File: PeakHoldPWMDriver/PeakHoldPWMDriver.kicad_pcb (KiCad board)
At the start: 2 copper layers, 74 parts, among them Q1 BSP78, Q16 SMD-MOSFET-N-CH-55V-2.1A-AO34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, Q17 TSM2309CX, Q19 SMD-MOSFET-N-CH-55V-2.1A-AO34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, Q2 BSP78, Q20 TSM2309CX, Q21 SMD-MOSFET-N-CH-55V-2.1A-AO34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, Q22 SMD-MOSFET-N-CH-55V-2.1A-AO34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, Q23 TSM2309CX, Q24 TSM2309CX, Q3 BSP78, Q4 BSP78, U1 LM2901, U10 74LS08, U2 74LS08, U3 LM78M05_TO220, U4 74HC74, U5 74LS08, U6 LTC6992, U7 74LS08, U8 74LS08, U9 74LS08

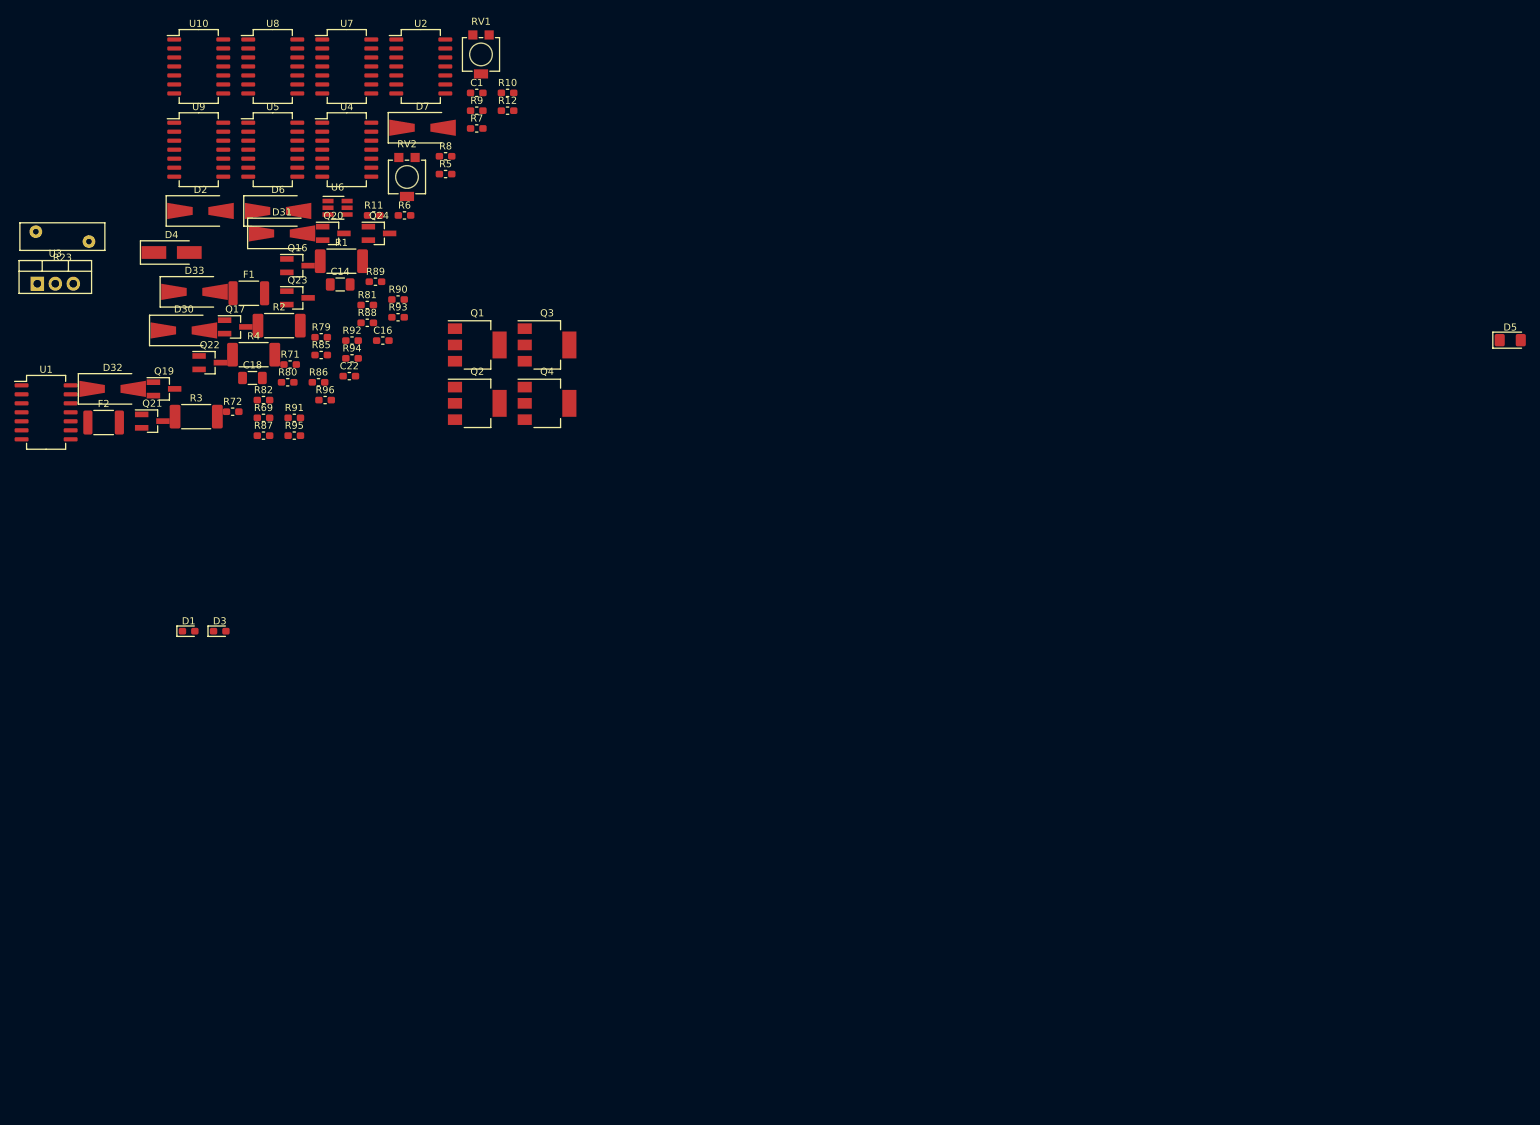
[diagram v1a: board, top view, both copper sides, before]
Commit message: Cleaned and updated the SPECTRE V0.5 Created separate Peak and Hold board.
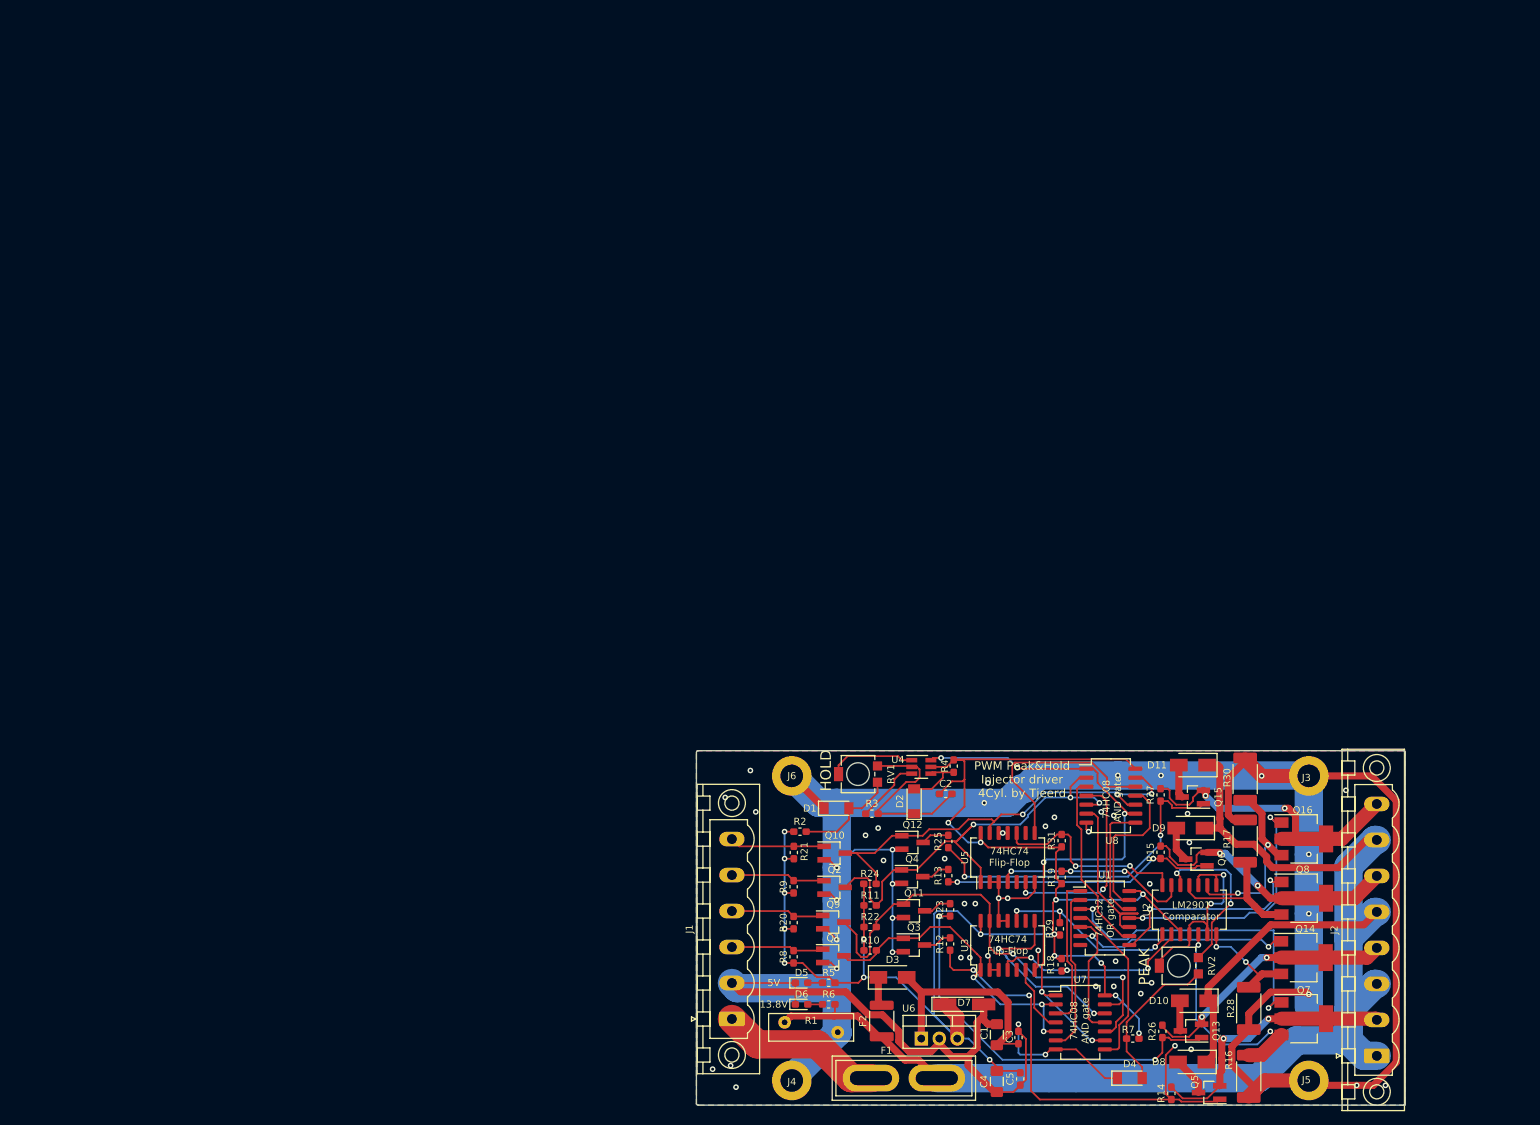
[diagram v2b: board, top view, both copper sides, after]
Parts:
- removed the D1 at (40.1, 49.2)
- removed the D2 at (41.7, -10.2)
- removed D30, D31, D32, D33: SS310, Diode_SMD:D_SMA-SMB_Universal_Handsoldering
- removed the F2 at (28.1, 19.7)
- removed Q17, Q20, Q23, Q24: TSM2309CX, Package_TO_SOT_SMD:SOT-23_Handsoldering
- removed Q19: SMD-MOSFET-N-CH-55V-2.1A-AO3422(SOT-23), Package_TO_SOT_SMD:SOT-23_Handsoldering
- removed the Q4 at (90.7, 17.0)
- removed the R1 at (61.6, -3.07)
- removed the R2 at (52.8, 6.03)
- removed the R3 at (41.1, 18.9)
- removed R72: 0R0, Resistor_SMD:R_0603_1608Metric_Pad1.05x0.95mm_HandSolder
- removed R79, R88, R95, R96: 10k, Resistor_SMD:R_0603_1608Metric_Pad1.05x0.95mm_HandSolder
- removed R80, R85, R89, R90: 1K, Resistor_SMD:R_0603_1608Metric_Pad1.05x0.95mm_HandSolder
- removed R81, R86, R91, R93: 470, Resistor_SMD:R_0603_1608Metric_Pad1.05x0.95mm_HandSolder
- removed R82, R87: 1K8, Resistor_SMD:R_0603_1608Metric_Pad1.05x0.95mm_HandSolder
- removed U10, U9: 74LS08, Package_SO:SO-14_5.3x10.2mm_P1.27mm
- removed the U2 at (72.8, -30.6)
- removed the U4 at (62.4, -18.8)
- removed the U8 at (51.9, -30.6)
- added D10: SS310, Diode_SMD:D_SMA, F.Cu at (182.0, 101.3)
- added D11: SS310, Diode_SMD:D_SMA, F.Cu at (181.9, 68.1)
- added D6: BLUE, LED_SMD:LED_0603_1608Metric_Pad1.05x0.95mm_HandSolder, F.Cu at (126.6, 101.9)
- added D7: D_Zener_Small, Diode_SMD:D_MiniMELF_Handsoldering, F.Cu at (149.6, 101.9)
- added D8: SS310, Diode_SMD:D_SMA, F.Cu at (181.8, 110.0)
- added D9: SS310, Diode_SMD:D_SMA, F.Cu at (181.5, 77.0)
- added F1: Fuse, Fuse:Fuse_Blade_ATO_directSolder, F.Cu at (136.4, 112.3)
- added J1: Screw_Terminal_01x06, Connector_Phoenix_MSTB:PhoenixContact_MSTBV_2,5_6-GF-5,08_1x06_P5.08mm_Vertical_ThreadedFlange, F.Cu at (116.8, 103.9)
- added J2: Screw_Terminal_01x08, Connector_Phoenix_MSTB:PhoenixContact_MSTBV_2,5_8-GF-5,08_1x08_P5.08mm_Vertical_ThreadedFlange, F.Cu at (207.8, 109.1)
- added J3: Mounting 3mm, MountingHole:MountingHole_3.2mm_M3_DIN965_Pad, F.Cu at (198.2, 69.6)
- added J4: Mounting 3mm, MountingHole:MountingHole_3.2mm_M3_DIN965_Pad, F.Cu at (125.2, 112.6)
- added J5: Mounting 3mm, MountingHole:MountingHole_3.2mm_M3_DIN965_Pad, F.Cu at (198.2, 112.6)
- added J6: Mounting 3mm, MountingHole:MountingHole_3.2mm_M3_DIN965_Pad, F.Cu at (125.2, 69.6)
- added Q10: AO3400, Package_TO_SOT_SMD:SOT-23_Handsoldering, F.Cu at (131.3, 80.5)
- added Q13: AO3401A, Package_TO_SOT_SMD:SOT-23_Handsoldering, F.Cu at (181.6, 105.6)
- added Q14: BSP78, Package_TO_SOT_SMD:SOT-223, F.Cu at (197.5, 95.2)
- added Q15: AO3401A, Package_TO_SOT_SMD:SOT-23_Handsoldering, F.Cu at (181.8, 72.6)
- added Q16: BSP78, Package_TO_SOT_SMD:SOT-223, F.Cu at (197.5, 78.5)
- added Q5: AO3401A, Package_TO_SOT_SMD:SOT-23_Handsoldering, F.Cu at (184.2, 114.3)
- added Q6: AO3401A, Package_TO_SOT_SMD:SOT-23_Handsoldering, F.Cu at (182.3, 81.3)
- added Q7: BSP78, Package_TO_SOT_SMD:SOT-223, F.Cu at (197.5, 103.9)
- added Q8: BSP78, Package_TO_SOT_SMD:SOT-223, F.Cu at (197.5, 86.9)
- added Q9: AO3400, Package_TO_SOT_SMD:SOT-23_Handsoldering, F.Cu at (131.1, 90.2)
- added R10: 10K, Resistor_SMD:R_0603_1608Metric_Pad1.05x0.95mm_HandSolder, F.Cu at (136.3, 94.2)
- added R11: 10K, Resistor_SMD:R_0603_1608Metric_Pad1.05x0.95mm_HandSolder, F.Cu at (136.3, 87.9)
- added R12: 1K8, Resistor_SMD:R_0603_1608Metric_Pad1.05x0.95mm_HandSolder, F.Cu at (147.6, 93.3)
- added R13: 1K8, Resistor_SMD:R_0603_1608Metric_Pad1.05x0.95mm_HandSolder, F.Cu at (147.3, 83.7)
- added R14: 470, Resistor_SMD:R_0603_1608Metric_Pad1.05x0.95mm_HandSolder, F.Cu at (178.8, 114.4)
- added R15: 470, Resistor_SMD:R_0603_1608Metric_Pad1.05x0.95mm_HandSolder, F.Cu at (177.3, 80.4)
- added R16: 0R1, Resistor_SMD:R_2512_6332Metric_Pad1.52x3.35mm_HandSolder, F.Cu at (189.7, 112.0)
- added R17: 0R1, Resistor_SMD:R_2512_6332Metric_Pad1.52x3.35mm_HandSolder, F.Cu at (189.2, 78.8)
- added R20: 1K, Resistor_SMD:R_0603_1608Metric_Pad1.05x0.95mm_HandSolder, F.Cu at (125.5, 90.3)
- added R21: 1K, Resistor_SMD:R_0603_1608Metric_Pad1.05x0.95mm_HandSolder, F.Cu at (125.5, 80.4)
- added R22: 10K, Resistor_SMD:R_0603_1608Metric_Pad1.05x0.95mm_HandSolder, F.Cu at (136.3, 90.9)
- added R24: 10K, Resistor_SMD:R_0603_1608Metric_Pad1.05x0.95mm_HandSolder, F.Cu at (136.3, 84.8)
- added R26: 470, Resistor_SMD:R_0603_1608Metric_Pad1.05x0.95mm_HandSolder, F.Cu at (177.5, 105.7)
- added R27: 470, Resistor_SMD:R_0603_1608Metric_Pad1.05x0.95mm_HandSolder, F.Cu at (177.3, 72.3)
- added R28: 0R1, Resistor_SMD:R_2512_6332Metric_Pad1.52x3.35mm_HandSolder, F.Cu at (189.7, 102.4)
- added R30: 0R1, Resistor_SMD:R_2512_6332Metric_Pad1.52x3.35mm_HandSolder, F.Cu at (189.2, 70.0)
- added R9: 1K, Resistor_SMD:R_0603_1608Metric_Pad1.05x0.95mm_HandSolder, F.Cu at (125.5, 85.3)
- added U3: 74LS74, Package_SO:SO-14_5.3x10.2mm_P1.27mm, F.Cu at (155.7, 93.5)
- added U5: 74LS74, Package_SO:SO-14_5.3x10.2mm_P1.27mm, F.Cu at (155.7, 81.1)
- added U7: 74LS08, Package_SO:SO-14_5.3x10.2mm_P1.27mm, F.Cu at (166.0, 104.4)
- C1: renamed from C14; footprint Capacitor_SMD:C_1206_3216Metric -> Capacitor_SMD:C_1206_3216Metric_Pad1.42x1.75mm_HandSolder
- C4: renamed from C18; footprint Capacitor_SMD:C_1206_3216Metric -> Capacitor_SMD:C_1206_3216Metric_Pad1.42x1.75mm_HandSolder
- D1: renamed from D6; value SS310 -> LL4148; footprint Diode_SMD:D_SMA-SMB_Universal_Handsoldering -> Diode_SMD:D_MiniMELF
- D2: renamed from D7; footprint Diode_SMD:D_SMA-SMB_Universal_Handsoldering -> Diode_SMD:D_MiniMELF
- D3: value BLUE -> 40V-1A; footprint LED_SMD:LED_0603_1608Metric_Pad1.05x0.95mm_HandSolder -> Diode_SMD:D_SMA
- D4: value D -> LL4148; footprint Diode_SMD:D_SMA_Handsoldering -> Diode_SMD:D_MiniMELF
- D5: value 5V1 -> BLUE; footprint Diode_SMD:D_1206_3216Metric_Pad1.42x1.75mm_HandSolder -> LED_SMD:LED_0603_1608Metric_Pad1.05x0.95mm_HandSolder
- F2: renamed from F1; footprint Resistor_SMD:R_1812_4532Metric_Pad1.30x3.40mm_HandSolder -> Fuse:Fuse_1812_4532Metric_Pad1.30x3.40mm_HandSolder
- Q1, Q2: value BSP78 -> AO3400; footprint Package_TO_SOT_SMD:SOT-223-3_TabPin2 -> Package_TO_SOT_SMD:SOT-23_Handsoldering
- Q11: renamed from Q21; value SMD-MOSFET-N-CH-55V-2.1A-AO3422(SOT-23) -> AO3422
- Q12: renamed from Q22; value SMD-MOSFET-N-CH-55V-2.1A-AO3422(SOT-23) -> AO3422
- Q3: value BSP78 -> AO3422; footprint Package_TO_SOT_SMD:SOT-223-3_TabPin2 -> Package_TO_SOT_SMD:SOT-23_Handsoldering
- Q4: renamed from Q16; value SMD-MOSFET-N-CH-55V-2.1A-AO3422(SOT-23) -> AO3422
- R4: value 0R1 -> 500k; footprint Resistor_SMD:R_2512_6332Metric_Pad1.52x3.35mm_HandSolder -> Resistor_SMD:R_0603_1608Metric_Pad1.05x0.95mm_HandSolder
- R8: value 500k -> 1K
- U1: renamed from U7; value 74LS08 -> 74LS32
- moved D4 178.6 mm to (172.9, 112.3)
- moved U2 176.0 mm to (181.4, 88.5), turned to 90 degrees
- moved U6 164.1 mm to (143.5, 106.7)
- moved RV2 162.1 mm to (179.9, 96.4), turned to 270 degrees
- moved U1 161.0 mm to (169.4, 89.7)
- moved R1 160.0 mm to (131.7, 105.8), turned to 180 degrees
- moved R7 155.9 mm to (173.4, 106.7), turned to 180 degrees
- moved U8 149.4 mm to (170.3, 72.4)
- moved R18 146.2 mm to (163.3, 96.3), turned to 270 degrees
- moved C4 144.6 mm to (154.2, 112.7), turned to 90 degrees
- moved C1 140.8 mm to (154.2, 106.1), turned to 270 degrees
- moved R29 139.7 mm to (163.1, 91.2), turned to 90 degrees
- moved C5 137.2 mm to (157.5, 112.4), turned to 90 degrees
- moved F2 136.2 mm to (137.9, 104.2), turned to 90 degrees
- moved R19 135.6 mm to (163.3, 83.9), turned to 90 degrees
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- renumbered C1 to C2, C16 to C3, C22 to C5, R23 to R1, R9 to R18, R10 to R19, R6 to R2, R92 to R23, R94 to R25, R11 to R29, R7 to R3, R12 to R31, R69 to R5, R71 to R6, R5 to R7, RV2 to RV1, RV1 to RV2, U1 to U2, U6 to U4, U3 to U6, U5 to U8
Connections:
- C1 pad 1: GND -> PWR_GND
- C1 pad 2: Net-(C14-Pad2) -> Net-(C1-Pad2)
- C2 pad 2: GND -> PWR_GND
- C3 pad 1: GND -> PWR_GND
- C3 pad 2: Net-(C14-Pad2) -> Net-(C1-Pad2)
- C4 pad 1: GND -> PWR_GND
- C5 pad 1: GND -> PWR_GND
- D1 pad 1: GND -> PWR_GND
- D2 pad 1: GND -> PWR_GND
- D2 pad 2: Net-(D7-Pad2) -> Net-(D2-Pad2)
- D3 pad 1: GND -> Net-(D3-Pad1)
- D3 pad 2: Net-(D3-Pad2) -> Net-(C1-Pad2)
- D4 pad 1: Net-(C14-Pad2) -> PWR_GND
- D4 pad 2: VBAT_F1 -> Net-(D4-Pad2)
- D5 pad 1: 5V -> PWR_GND
- D5 pad 2: GND -> Net-(D5-Pad2)
- F2 pad 2: VBAT_F1 -> Net-(D3-Pad1)
- Q1 pad 1: Net-(Q1-Pad1) -> INJ1
- Q1 pad 2: INJ1-OUT -> PWR_GND
- Q1 pad 3: Net-(Q1-Pad3) -> inv_INJ1
- Q11 pad 1: PE12 -> inv_INJ2
- Q11 pad 2: GND -> PWR_GND
- Q12 pad 1: PE15 -> inv_INJ4
- Q12 pad 2: GND -> PWR_GND
- Q2 pad 1: Net-(Q2-Pad1) -> INJ3
- Q2 pad 2: INJ3-OUT -> PWR_GND
- Q2 pad 3: Net-(Q2-Pad3) -> inv_INJ3
- Q3 pad 1: Net-(Q3-Pad1) -> inv_INJ1
- Q3 pad 2: INJ2-OUT -> PWR_GND
- Q4 pad 1: PE10 -> inv_INJ3
- Q4 pad 2: GND -> PWR_GND
- R1 pad 1: GND -> PWR_GND
- R19 pad 2: Net-(R10-Pad2) -> Net-(R19-Pad2)
- R29 pad 2: Net-(R11-Pad2) -> Net-(R29-Pad2)
- R3 pad 2: GND -> PWR_GND
- R4 pad 1: Net-(Q4-Pad3) (its old number) -> 5V
- R4 pad 2: GND -> Net-(D2-Pad2)
- R5 pad 1: Net-(D1-Pad2) (its old number) -> Net-(D5-Pad2)
- R6 pad 1: Net-(D3-Pad2) -> Net-(D6-Pad2)
- R7 pad 2: Net-(D2-Pad2) -> Net-(D4-Pad2)
- R8 pad 2: Net-(D7-Pad2) -> INJ1
- RV1 pad 3: GND -> PWR_GND
- RV2 pad 1: Net-(D2-Pad2) -> Net-(D4-Pad2)
- RV2 pad 3: GND -> PWR_GND
- U1 pad 10: (no net) -> Net-(U1-Pad10)
- U1 pad 12: Net-(U2-Pad8) -> Net-(U1-Pad12)
- U1 pad 3: Net-(Q1-Pad1) -> Net-(Q7-Pad1)
- U1 pad 4: Net-(U5-Pad8) (its old number) -> Net-(U1-Pad4)
- U1 pad 6: Net-(Q2-Pad1) -> Net-(Q14-Pad1)
- U1 pad 7: GND -> PWR_GND
- U1 pad 8: (no net) -> Net-(Q8-Pad1)
- U1 pad 9: (no net) -> Net-(U1-Pad9)
- U2 pad 1: Net-(R10-Pad2) -> Net-(R29-Pad2)
- U2 pad 11: Net-(Q3-Pad3) -> Net-(Q8-Pad3)
- U2 pad 12: GND -> PWR_GND
- U2 pad 13: Net-(R11-Pad2) -> Net-(R19-Pad2)
- U2 pad 5: Net-(Q1-Pad3) -> Net-(Q7-Pad3)
- U2 pad 7: Net-(Q2-Pad3) -> Net-(Q14-Pad3)
- U2 pad 9: Net-(Q4-Pad3) (its old number) -> Net-(Q16-Pad3)
- U4 pad 2: GND -> PWR_GND
- U4 pad 4: Net-(D7-Pad2) -> Net-(D2-Pad2)
- U6 pad 1: Net-(C14-Pad2) -> Net-(C1-Pad2)
- U6 pad 2: GND -> PWR_GND
- U8 pad 10: PE10 -> inv_INJ4
- U8 pad 13: PE15 -> inv_INJ4
- U8 pad 2: PE12 -> inv_INJ3
- U8 pad 3: Net-(U5-Pad3) -> Net-(U1-Pad9)
- U8 pad 5: PE12 -> inv_INJ3
- U8 pad 6: Net-(U5-Pad6) (its old number) -> Net-(U1-Pad10)
- U8 pad 7: GND -> PWR_GND
- U8 pad 8: Net-(U5-Pad8) (its old number) -> Net-(U1-Pad12)
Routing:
- net PWR_GND: track 0.00 -> 509.7 mm, vias 0 -> 56
- net 5V: track 0.00 -> 253.7 mm, vias 0 -> 18
- net VBAT: track 0.00 -> 213.4 mm
- net PWM: track 0.00 -> 84.8 mm, vias 0 -> 6
- net inv_INJ2: track 0.00 -> 70.8 mm, vias 0 -> 2
- net Net-(Q5-Pad1): track 0.00 -> 64.8 mm, vias 0 -> 3
- net inv_INJ3: track 0.00 -> 64.8 mm, vias 0 -> 3
- net inv_INJ4: track 0.00 -> 63.4 mm, vias 0 -> 3
- net Net-(Q13-Pad1): track 0.00 -> 56.4 mm, vias 0 -> 2
- net Net-(Q15-Pad1): track 0.00 -> 47.6 mm, vias 0 -> 2
- net inv_INJ1: track 0.00 -> 46.0 mm, vias 0 -> 3
- net Net-(Q7-Pad1): track 0.00 -> 44.0 mm, vias 0 -> 2
- net INJ4-OUT: track 0.00 -> 42.3 mm, vias 0 -> 2
- net Net-(Q6-Pad1): track 0.00 -> 38.6 mm, vias 0 -> 2
- net INJ1-OUT: track 0.00 -> 38.0 mm, vias 0 -> 2
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- added copper zone on B.Cu, net PWR_GND
- added copper zone on F.Cu, net PWR_GND
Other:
- board outline added: 100.1 x 50 mm
- board text added: "13.8V"
- board text added: "5V"
- board text added: "74HC08 AND gate"
- board text added: "74HC32 OR gate"
- board text added: "74HC74 Flip-Flop"
- board text added: "HOLD"
- board text added: "LM2901 Comparator"
- board text added: "PEAK"
- board text added: "PWM Peak&Hold Injector driver 4Cyl. by Tjeerd"
